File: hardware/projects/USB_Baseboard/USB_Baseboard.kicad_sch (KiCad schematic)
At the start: 7 parts, among them J3 USB4720-03-A, U8 USBLC6-2SC6

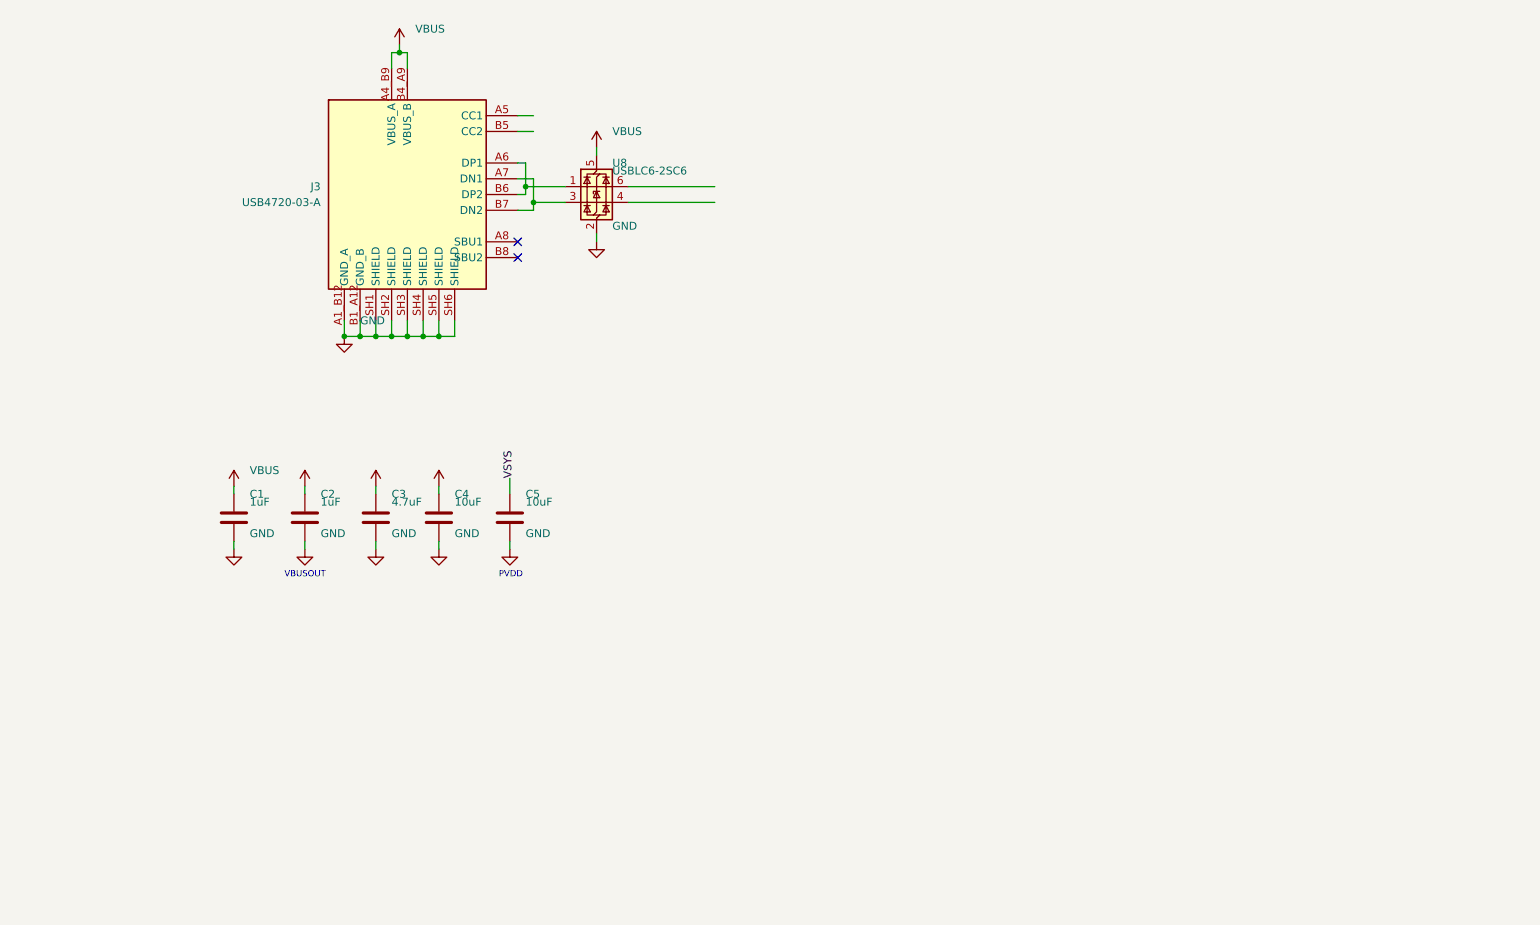
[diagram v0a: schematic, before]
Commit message: hardware: complete modular main-board and USB schematics
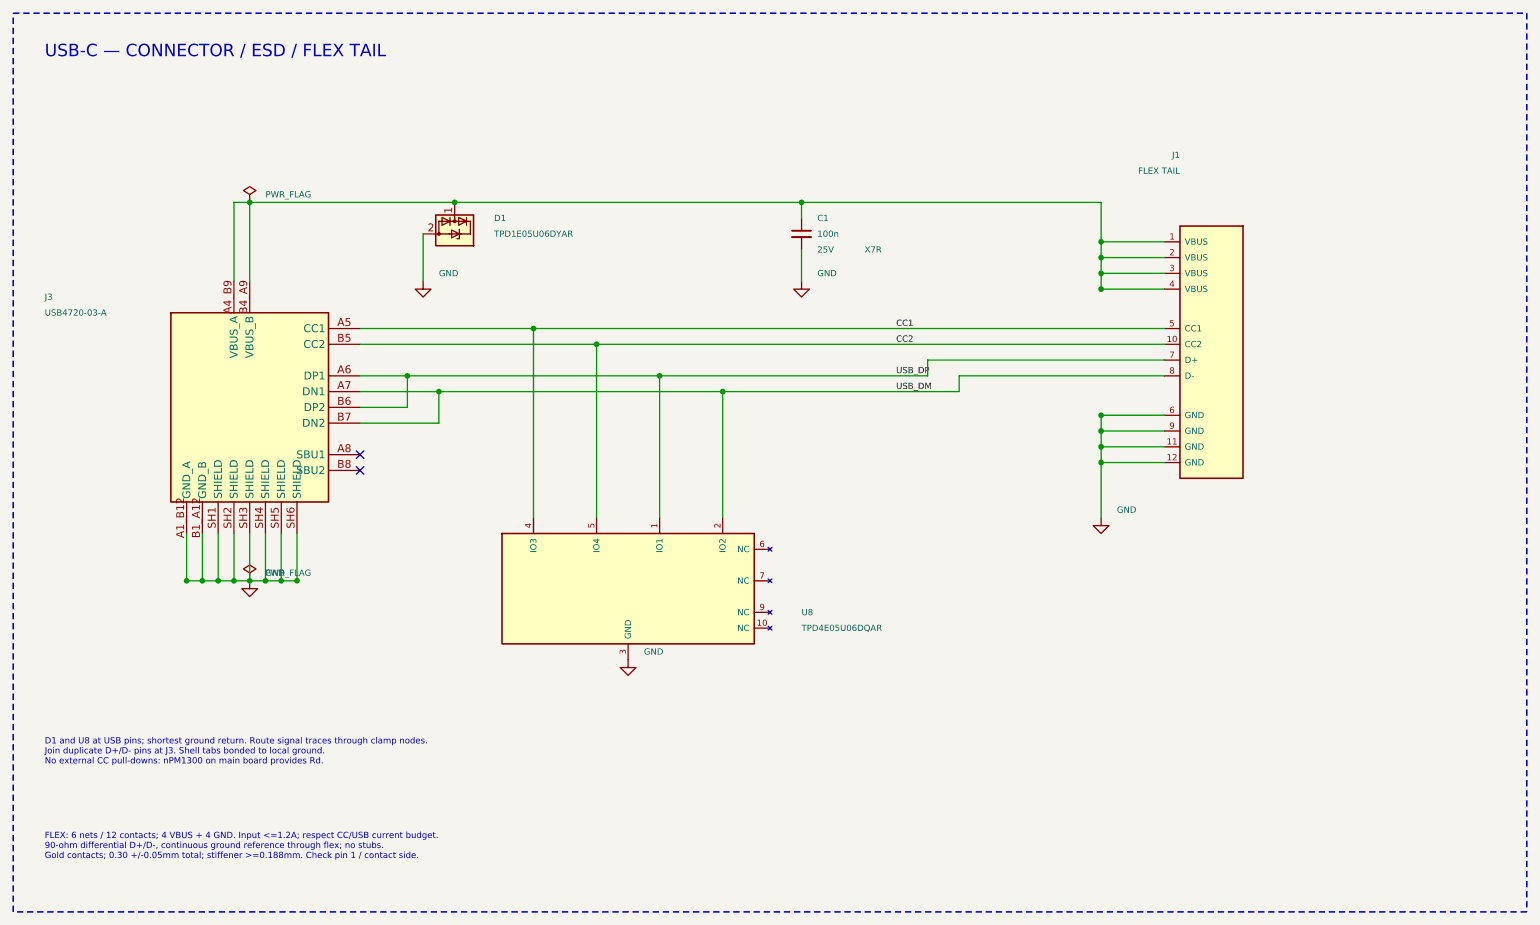
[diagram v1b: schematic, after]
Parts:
- removed C1, C2: 1uF, Capacitor_SMD:C_0402_1005Metric, symbol Device:C
- removed C3: 4.7uF, Capacitor_SMD:C_0603_1608Metric, symbol Device:C
- removed C4, C5: 10uF, Capacitor_SMD:C_0603_1608Metric, symbol Device:C
- removed U8: USBLC6-2SC6, Package_TO_SOT_SMD:SOT-23-6, symbol Power_Protection:USBLC6-2SC6
- added C1: 100n, Capacitor_SMD:C_0402_1005Metric, symbol Device:C_Small
- added D1: TPD1E05U06DYAR, Diode_SMD:D_SOD-523, symbol Power_Protection:TPD1E05U06DYA
- added J1: FLEX TAIL, obc:FPC_12_P0.5_FH12_Tail, symbol obc:USB_FLEX_12
- added U8: TPD4E05U06DQAR, obc:TI_DQA0010A_USON-10_2.5x1.0mm_P0.5mm, symbol obc:TPD4E05U06DQA
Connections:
- net GND: now also C1.2, D1.2 (GND), J1.11 (GND), J1.12 (GND), J1.6 (GND), J1.9 (GND), U8.3 (GND), U8.8 (GND)
- net CC1: now reaches J3.A5 (CC1)
- net CC1: now also J1.5 (CC1), U8.4 (IO3)
- net USB_DP: now reaches J3.A6 (DP1), J3.B6 (DP2)
- net USB_DP: now also J1.7 (D+), U8.1 (IO1)
- net USB_DM: now reaches J3.A7 (DN1), J3.B7 (DN2)
- net USB_DM: now also J1.8 (D-), U8.2 (IO2)
- net CC2: now reaches J3.B5 (CC2)
- net CC2: now also J1.10 (CC2), U8.5 (IO4)
- net VBUS: no longer names the net of J3.A4_B9 (VBUS_A), J3.B4_A9 (VBUS_B)
- net VBUS: now also C1.1, D1.1 (I/O), J1.1 (VBUS), J1.2 (VBUS), J1.3 (VBUS), J1.4 (VBUS)
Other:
- note added: "D1 and U8 at USB pins; shortest ground return. Route signal traces through clamp nodes. Join duplicate D+/D- pins at J3. Shell tabs bonded to local ground. No external CC pull-downs: nPM1300 on main board provides Rd."
- note added: "FLEX: 6 nets / 12 contacts; 4 VBUS + 4 GND. Input <=1.2A; respect CC/USB current budget. 90-ohm differential D+/D-, continuous ground reference through flex; no stubs. Gold contacts; 0.30 +/-0.05mm total; stiffener >=0.188mm. Check pin 1 / contact side."
- note added: "USB-C — CONNECTOR / ESD / FLEX TAIL"
- note removed: "PVDD"
- note removed: "VBUSOUT"
- company: (none) -> OpenBikeComputer
- title: (none) -> OpenBikeComputer — USB rigid-flex
- moved on the sheet: J3

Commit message: fix(hardware): apply schematic review and peripheral pin mapping
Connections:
- net CC1: now also J1.4 (CC1); no longer J1.5 (CC1)
- net CC2: now also J1.9 (CC2); no longer J1.10 (CC2)
- net GND: now also J1.1 (GND), J1.5 (GND), J1.8 (GND); no longer J1.11 (GND), J1.6 (GND), J1.9 (GND)
- net USB_DM: now also J1.7 (D-); no longer J1.8 (D-)
- net USB_DP: now also J1.6 (D+); no longer J1.7 (D+)
- net at C1.1, D1.1 (I/O), J1.2 (VBUS)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: now also J1.10 (VBUS), J1.11 (VBUS); no longer J1.1 (VBUS), J1.4 (VBUS)

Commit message: hardware: name critical nets and ground connector tabs
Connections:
- net GND: now also J1.MP (SHIELD)

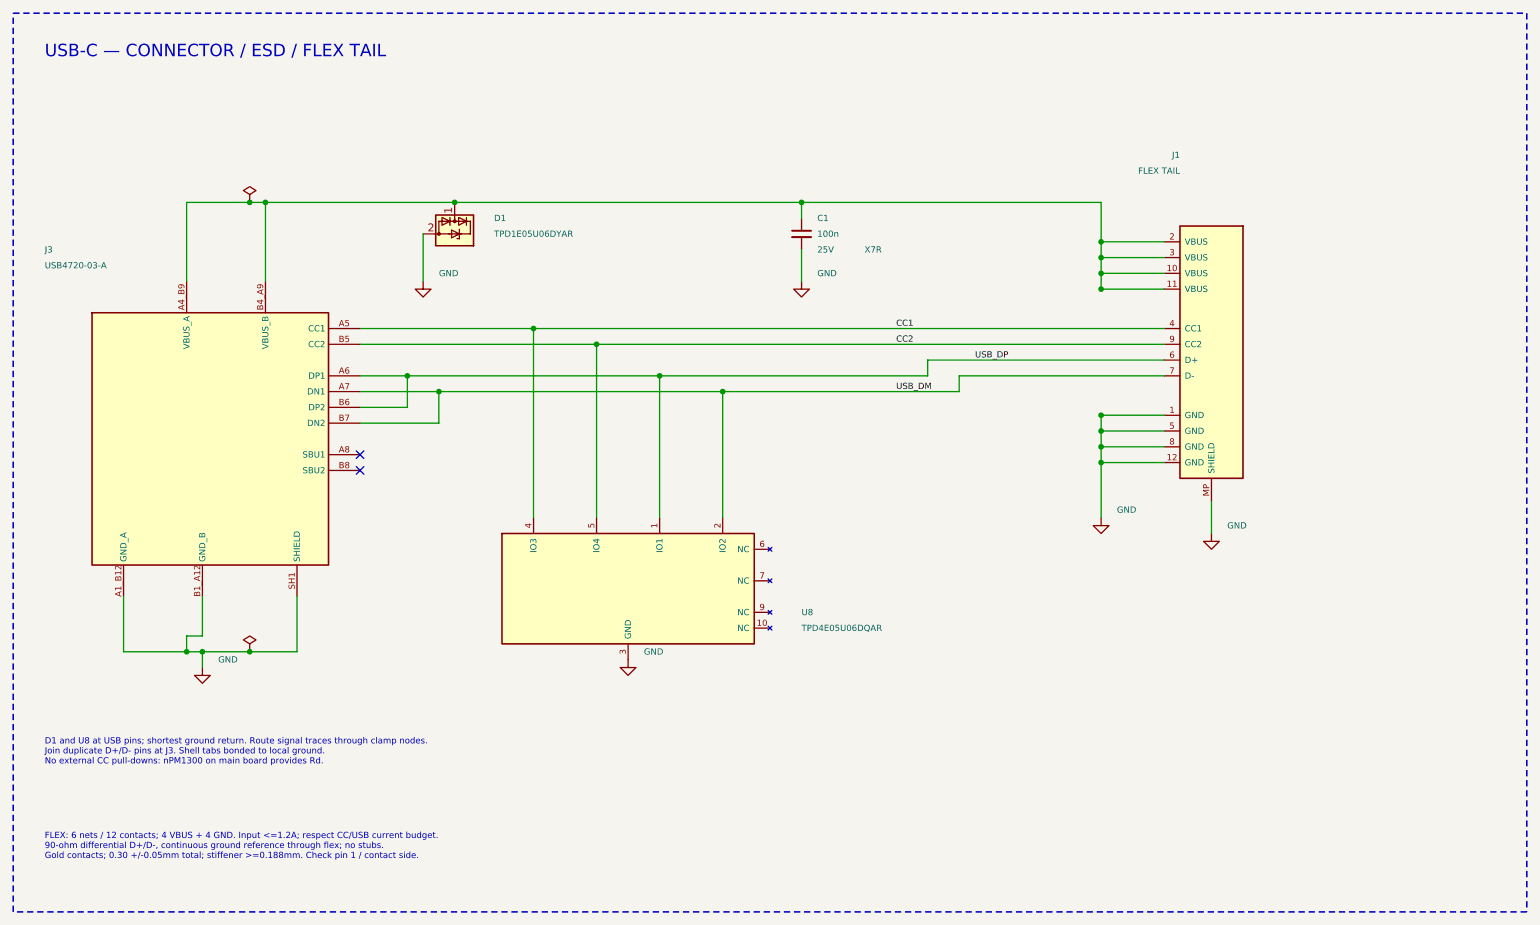
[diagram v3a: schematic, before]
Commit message: hardware: consolidate USB baseboard, flex and connector assets
Bring the saved USB4730 baseboard, separate USB flex and battery metadata into the current shielded main-board branch. Preserve the main-board placement and circuit. Retain the existing connector assets. The saved FH12 flex tail still needs alignment with the main-board FH34SRJ connector before fabrication. Public docs unchanged.
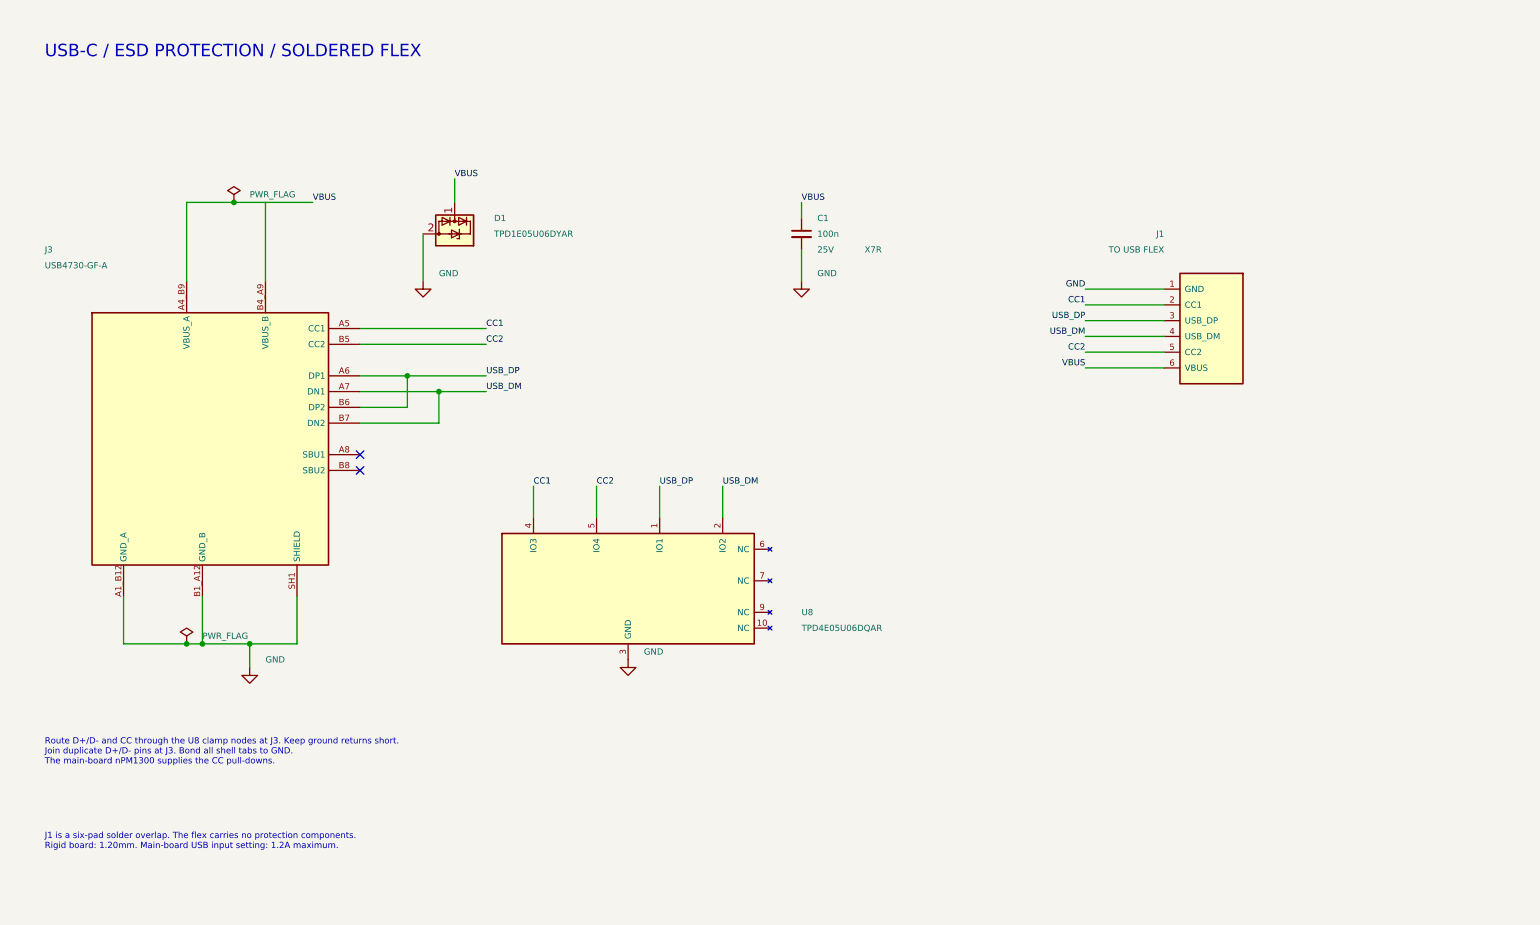
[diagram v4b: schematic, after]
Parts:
- J1: value FLEX TAIL -> TO USB FLEX; footprint obc:FPC_12_P0.5_FH12_Tail -> obc:USB_Flex_Solder_6; symbol obc:USB_FLEX_12 -> obc:USB_FLEX_SOLDER_6; FPC Thickness 0.30 +/-0.05mm at stiffened tail -> (none)
- J3: value USB4720-03-A -> USB4730-GF-A; footprint obc:GCT_USB4720-03-A_REVA -> obc:GCT_USB4730-GF-A; symbol obc:USB4720-03-A -> obc:USB4730-GF-A; MAXIMUM_PACKAGE_HEIGHT 2.22mm -> 4.66mm; MPN USB4720-03-A -> USB4730-GF-A; SNAPEDA_PN USB4720-03-A -> (none)
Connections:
- net CC1: now also J1.2 (CC1); no longer J1.4 (CC1)
- net CC2: now also J1.5 (CC2); no longer J1.9 (CC2)
- net GND: no longer J1.12 (GND), J1.5 (GND), J1.8 (GND), J1.MP (SHIELD), J3.SH5 (SHIELD), J3.SH6 (SHIELD)
- net USB_DM: now also J1.4 (USB_DM); no longer J1.7 (D-)
- net USB_DP: now also J1.3 (USB_DP); no longer J1.6 (D+)
- net VBUS: now reaches C1.1, D1.1 (I/O), J3.A4_B9 (VBUS_A), J3.B4_A9 (VBUS_B)
- net VBUS: now also J1.6 (VBUS); no longer J1.10 (VBUS), J1.11 (VBUS), J1.2 (VBUS), J1.3 (VBUS)
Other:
- note added: "J1 is a six-pad solder overlap. The flex carries no protection components. Rigid board: 1.20mm. Main-board USB input setting: 1.2A maximum."
- note added: "Route D+/D- and CC through the U8 clamp nodes at J3. Keep ground returns short. Join duplicate D+/D- pins at J3. Bond all shell tabs to GND. The main-board nPM1300 supplies the CC pull-downs."
- note added: "USB-C / ESD PROTECTION / SOLDERED FLEX"
- note removed: "D1 and U8 at USB pins; shortest ground return. Route signal traces through clamp nodes. Join duplicate D+/D- pins at J3. Shell tabs bonded to local ground. No external CC pull-downs: nPM1300 on main board provides Rd."
- note removed: "FLEX: 6 nets / 12 contacts; 4 VBUS + 4 GND. Input <=1.2A; respect CC/USB current budget. 90-ohm differential D+/D-, continuous ground reference through flex; no stubs. Gold contacts; 0.30 +/-0.05mm total; stiffener >=0.188mm. Check pin 1 / contact side."
- note removed: "USB-C — CONNECTOR / ESD / FLEX TAIL"
- title: OpenBikeComputer — USB rigid-flex -> OpenBikeComputer - USB daughterboard

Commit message: hardware: add editable KiCad BOM and schematic exports
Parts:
- C1: MPN (none) -> GRM155R71E104KE14D; Manufacturer (none) -> Murata; Mouser (none) -> https://www.mouser.de/de/ProductDetail/Murata-Electronics/G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; Price breaks EUR (none) -> 1:0.086;10:0.013;100:0.011;500:0.008;1000:0.007;2500:0.006;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; Price checked (none) -> 2026-10-02; Price source (none) -> https://www.mouser.de/de/ProductDetail/Murata-Electronics/G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
- D1: Mouser (none) -> https://lv.mouser.com/lv/ProductDetail/Texas-Instruments/TP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; Price breaks EUR (none) -> 1:0.464;10:0.29;100:0.184;500:0.147;1000:0.124; Price checked (none) -> 2026-10-02; Price source (none) -> https://lv.mouser.com/lv/ProductDetail/Texas-Instruments/TP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
- J3: Mouser (none) -> https://www.mouser.de/ProductDetail/GCT/USB4730-GF-A?qs=Z%2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; Price breaks EUR (none) -> 1:1.51;10:1.29;25:1.15;100:1.10; Price checked (none) -> 2026-10-02; Price source (none) -> https://www.mouser.de/ProductDetail/GCT/USB4730-GF-A?qs=Z%2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
- U8: Mouser (none) -> https://eu.mouser.com/en/ProductDetail/Texas-Instruments/TP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; Price breaks EUR (none) -> 1:0.636;10:0.302;100:0.252;500:0.192;1000:0.181; Price checked (none) -> 2026-10-02; Price source (none) -> https://eu.mouser.com/en/ProductDetail/Texas-Instruments/TP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; Sourcing notes (none) -> Backorder shown; confirm delivery.
